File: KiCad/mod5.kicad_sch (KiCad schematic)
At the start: 46 parts, among them M10 Fan_4pin, M9 Fan_4pin

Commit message: Fix some diodes and resistors
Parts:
- D15, D16: value 1N5819WS -> B0520W
- R159: value R_Small -> 21.5k
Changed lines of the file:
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@@
 			)
 		)
-		(property "Value" "1N5819WS"
+		(property "Value" "B0520W"
 			(at 386.08 43.18 90)
 			(effects
@@
 			)
 		)
-		(property "Value" "1N5819WS"
+		(property "Value" "B0520W"
 			(at 331.47 43.18 90)
 			(effects
@@
 			)
 		)
-		(property "Value" "R_Small"
+		(property "Value" "21.5k"
 			(at 381 57.1499 0)
 			(effects

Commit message: Add external BIOS flash
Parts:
- added C327: 100nF, symbol Device:C_Small
- added R208, R209, R210: 10k, symbol Device:R_Small
- added U15: W25Q128JVS, Package_SO:SOIC-8_5.3x5.3mm_P1.27mm, symbol Memory_Flash:W25Q128JVS
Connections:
- net +3V3: now also C327.1, R208.1, R210.1, U15.8 (VCC)
- net GND: now also C327.2, R209.2, U15.4 (GND)
- net at A5.133 (~{BIOS_SEL}): now also R209.1
- net at A5.153 (SPI_IO3): now also R208.2, U15.7 (~{HOLD}/~{RESET}/IO_{3})
- net at A5.155 (SPI_CLK): now also U15.6 (CLK)
- net at A5.159 (SPI_MOSI/SPI_IO0): now also U15.5 (DI/IO_{0})
- net at A5.161 (SPI_IO2): now also R210.2, U15.3 (~{WP}/IO_{2})
- net at A5.163 (SPI_MISO/SPI_IO1): now also U15.2 (DO/IO_{1})
- net at A5.165 (~{SPI_CS}): now also U15.1 (~{CS})
- no-connect marks 1 -> 2

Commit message: Remove 0.95V Power Supply, Replace 3.3V Standby Power Supply
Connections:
- no-connect marks 2 -> 109

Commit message: Work though ERC errors
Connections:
- net PCIE_X4.SMBCLK renamed ETH.SMBCLK
- net PCIE_X4.SMBDAT renamed ETH.SMBDAT
- no-connect marks 109 -> 112
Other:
- moved on the sheet: R28

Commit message: Re-annotate components
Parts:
- C125: renamed from C113; value 100nF -> 220nF
- C126: renamed from C114; value 100nF -> 220nF
- renumbered C93 to C105, C94 to C106, C95 to C107, C96 to C108, C97 to C109, C98 to C110, C99 to C111, C100 to C112, C101 to C113, C102 to C114, C103 to C115, C104 to C116, C105 to C117, C106 to C118, C107 to C119, C108 to C120, C109 to C121, C110 to C122, C111 to C123, C112 to C124, C296 to C127, C327 to C128, C297 to C129, D21 to D17, D26 to D18, D15 to D19, D16 to D20, R167 to R81, R25 to R82, R26 to R83, R27 to R84, R28 to R85, R208 to R86, R209 to R87, R29 to R88, R30 to R89, R210 to R90, R156 to R91, R157 to R92, R180 to R93, R158 to R94, R159 to R95, R160 to R96, R161 to R97, R162 to R98, U15 to U5

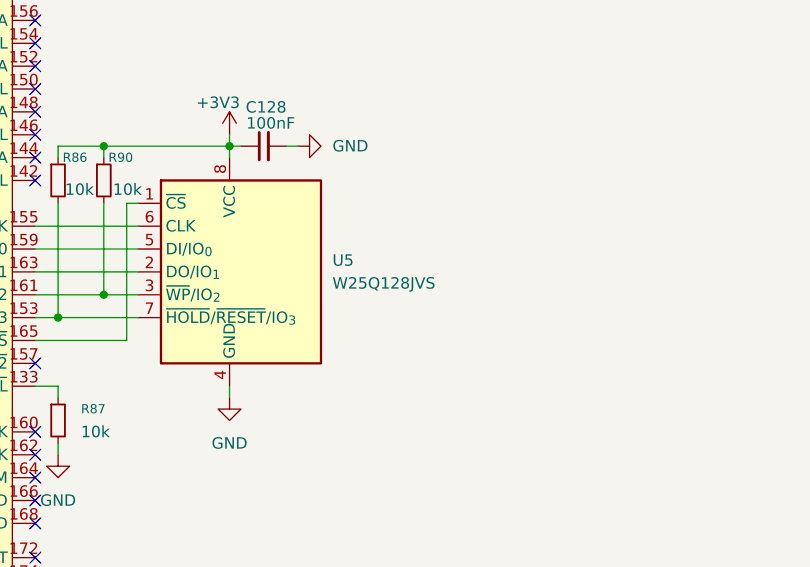
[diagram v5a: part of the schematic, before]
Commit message: Add TVS diodes for ESD protection
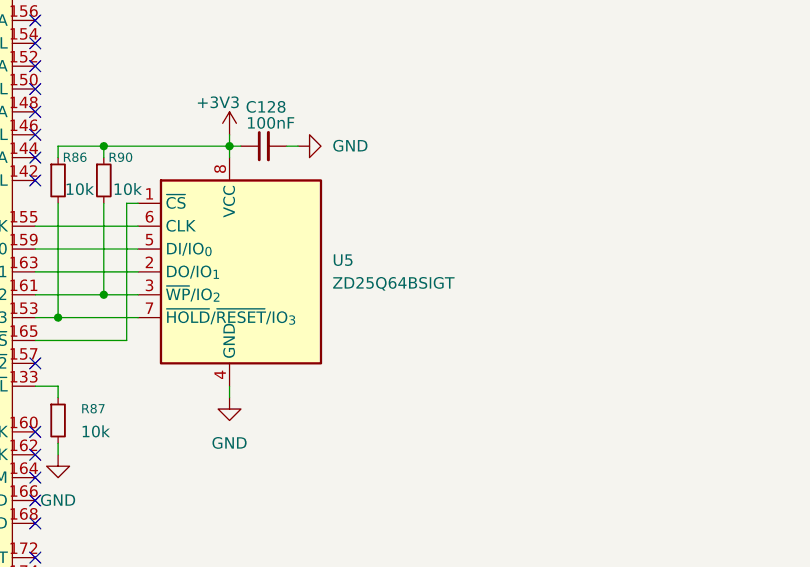
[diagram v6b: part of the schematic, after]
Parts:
- U5: value W25Q128JVS -> ZD25Q64BSIGT
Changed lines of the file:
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@@
 			)
 		)
-		(property "Value" "W25Q128JVS"
+		(property "Value" "ZD25Q64BSIGT"
 			(at 350.52 257.8099 0)
 			(effects

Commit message: Add more footprints
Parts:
- A5: footprint Module_LattePanda:LattePanda_Module_H8.0mm_Horizontal -> 124B-150A02:ATTEND_124B-150A02
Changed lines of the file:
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@@
 			)
 		)
-		(property "Footprint" "Module_LattePanda:LattePanda_Module_H8.0mm_Horizontal"
+		(property "Footprint" "124B-150A02:ATTEND_124B-150A02"
 			(at 276.86 193.04 0)
 			(effects

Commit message: Add more footprints
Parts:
- C105, C106, C107, C108, C109, C110, C111, C112, C113, C114, C115, C116, C117, C118, C119, C120, C121, C122, C123, C124, C125, C126, C127, C128, C129: footprint (none) -> Capacitor_SMD:C_0603_1608Metric
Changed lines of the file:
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@@
 			)
 		)
-		(property "Footprint" ""
+		(property "Footprint" "Capacitor_SMD:C_0603_1608Metric"
 			(at 227.33 144.78 0)
 			(effects
@@
 			)
 		)
-		(property "Footprint" ""
+		(property "Footprint" "Capacitor_SMD:C_0603_1608Metric"
 			(at 227.33 154.94 0)
 			(effects
@@
 			)
 		)
-		(property "Footprint" ""
+		(property "Footprint" "Capacitor_SMD:C_0603_1608Metric"
 			(at 227.33 165.1 0)
 			(effects
@@
 			)
 		)
-		(property "Footprint" ""
+		(property "Footprint" "Capacitor_SMD:C_0603_1608Metric"
 			(at 227.33 137.16 0)
 			(effects
@@
 			)
 		)
-		(property "Footprint" ""
+		(property "Footprint" "Capacitor_SMD:C_0603_1608Metric"
 			(at 227.33 167.64 0)
 			(effects
@@
 			)
 		)
-		(property "Footprint" ""
+		(property "Footprint" "Capacitor_SMD:C_0603_1608Metric"
 			(at 227.33 160.02 0)
 			(effects
@@
 			)
 		)
-		(property "Footprint" ""
+		(property "Footprint" "Capacitor_SMD:C_0603_1608Metric"
 			(at 227.33 177.8 0)
 			(effects
@@
 			)
 		)
-		(property "Footprint" ""
+		(property "Footprint" "Capacitor_SMD:C_0603_1608Metric"
 			(at 342.9 242.57 0)
 			(effects
@@
 			)
 		)
-		(property "Footprint" ""
+		(property "Footprint" "Capacitor_SMD:C_0603_1608Metric"
 			(at 227.33 170.18 0)
 			(effects
@@
 			)
 		)
-		(property "Footprint" ""
+		(property "Footprint" "Capacitor_SMD:C_0603_1608Metric"
 			(at 227.33 111.76 0)
 			(effects
@@
 			)
 		)
-		(property "Footprint" ""
+		(property "Footprint" "Capacitor_SMD:C_0603_1608Metric"
 			(at 227.33 121.92 0)
 			(effects
@@
 			)
 		)
-		(property "Footprint" ""
+		(property "Footprint" "Capacitor_SMD:C_0603_1608Metric"
 			(at 374.65 40.64 0)
 			(effects
@@
 			)
 		)
-		(property "Footprint" ""
+		(property "Footprint" "Capacitor_SMD:C_0603_1608Metric"
 			(at 227.33 147.32 0)
 			(effects
@@
 			)
 		)
-		(property "Footprint" ""
+		(property "Footprint" "Capacitor_SMD:C_0603_1608Metric"
 			(at 227.33 91.44 0)
 			(effects
@@
 			)
 		)
-		(property "Footprint" ""
+		(property "Footprint" "Capacitor_SMD:C_0603_1608Metric"
 			(at 227.33 172.72 0)
 			(effects
@@
 			)
 		)
-		(property "Footprint" ""
+		(property "Footprint" "Capacitor_SMD:C_0603_1608Metric"
 			(at 227.33 157.48 0)
 			(effects
@@
 			)
 		)
-		(property "Footprint" ""
+		(property "Footprint" "Capacitor_SMD:C_0603_1608Metric"
 			(at 227.33 162.56 0)
 			(effects
@@
 			)
 		)
-		(property "Footprint" ""
+		(property "Footprint" "Capacitor_SMD:C_0603_1608Metric"
 			(at 227.33 104.14 0)
 			(effects
@@
 			)
 		)
-		(property "Footprint" ""
+		(property "Footprint" "Capacitor_SMD:C_0603_1608Metric"
 			(at 227.33 180.34 0)
 			(effects
@@
 			)
 		)
-		(property "Footprint" ""
+		(property "Footprint" "Capacitor_SMD:C_0603_1608Metric"
 			(at 227.33 101.6 0)
 			(effects
@@
 			)
 		)
-		(property "Footprint" ""
+		(property "Footprint" "Capacitor_SMD:C_0603_1608Metric"
 			(at 323.85 40.64 0)
 			(effects
@@
 			)
 		)
-		(property "Footprint" ""
+		(property "Footprint" "Capacitor_SMD:C_0603_1608Metric"
 			(at 227.33 114.3 0)
 			(effects
@@
 			)
 		)
-		(property "Footprint" ""
+		(property "Footprint" "Capacitor_SMD:C_0603_1608Metric"
 			(at 227.33 93.98 0)
 			(effects
@@
 			)
 		)
-		(property "Footprint" ""
+		(property "Footprint" "Capacitor_SMD:C_0603_1608Metric"
 			(at 227.33 134.62 0)
 			(effects
@@
 			)
 		)
-		(property "Footprint" ""
+		(property "Footprint" "Capacitor_SMD:C_0603_1608Metric"
 			(at 227.33 124.46 0)
 			(effects
